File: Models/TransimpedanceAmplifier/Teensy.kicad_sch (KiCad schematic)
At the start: 5 parts, among them J11 Conn_01x24_Pin, J13 Conn_01x24_Pin, U13 Teensy4.1

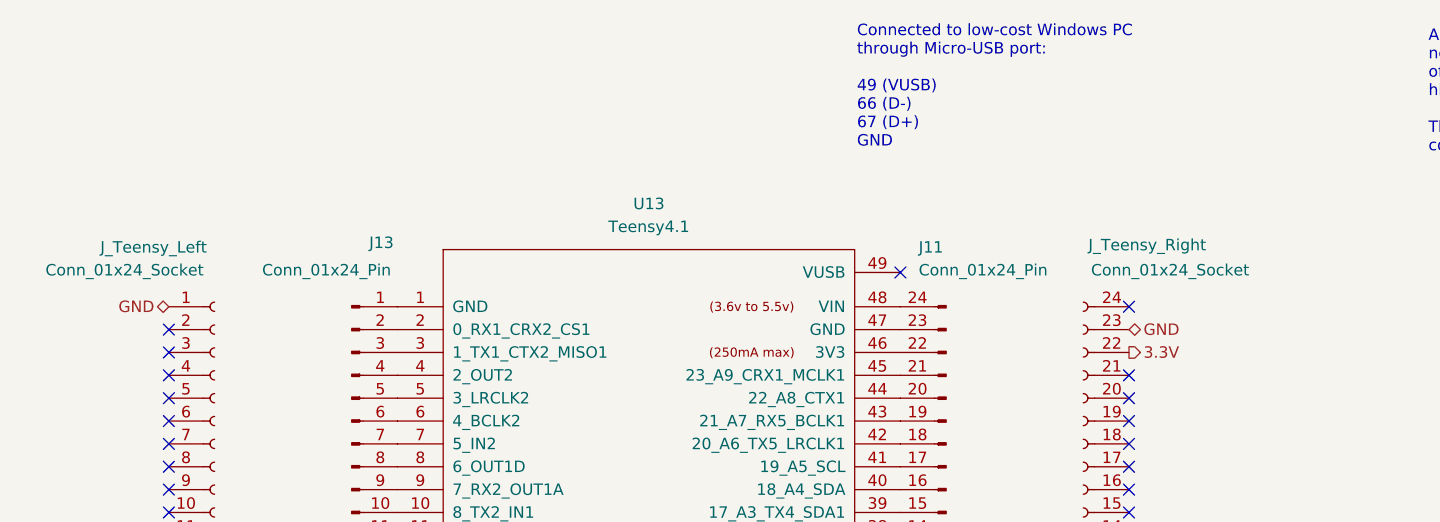
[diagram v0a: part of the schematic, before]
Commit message: Overhauled all of the annotations
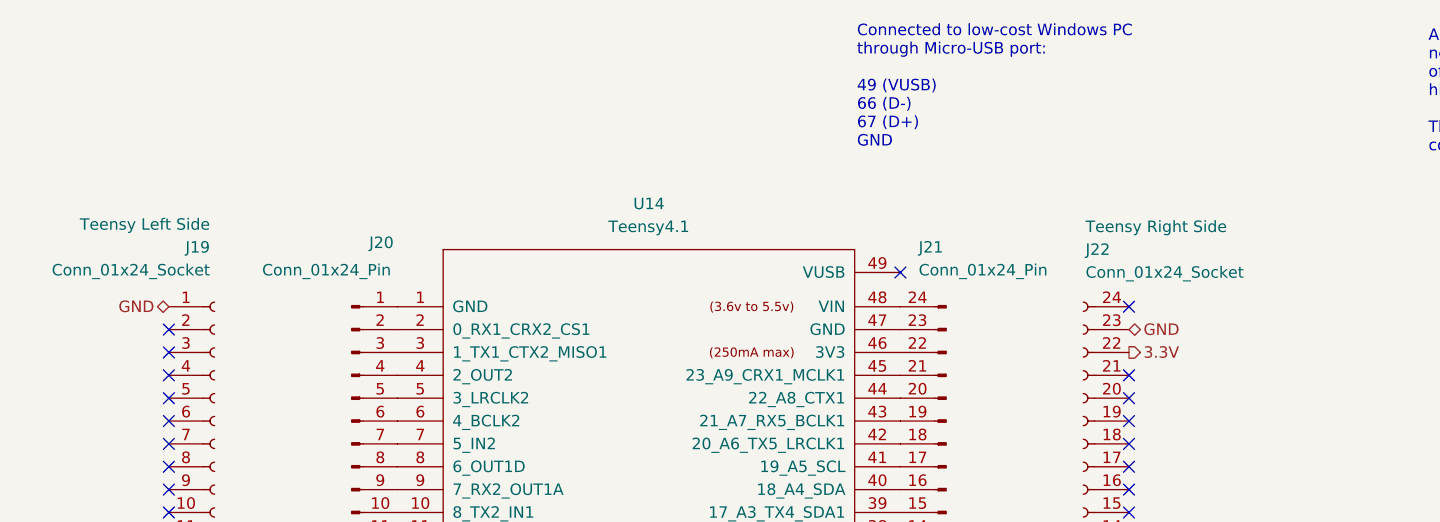
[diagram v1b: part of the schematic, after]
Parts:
- renumbered J_Teensy_Left to J19, J13 to J20, J11 to J21, J_Teensy_Right to J22, U13 to U14
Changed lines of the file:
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@@
 		(on_board yes)
 		(dnp no)
-		(property "Reference" "J_Teensy_Right"
-			(at 159.512 62.992 0)
-			(effects
-				(font
-					(size 1.27 1.27)
-				)
+		(property "Reference" "J22"
+			(at 152.654 63.5 0)
+			(effects
+				(font
+					(size 1.27 1.27)
+				)
+				(justify right)
 			)
 		)
 		(property "Value" "Conn_01x24_Socket"
-			(at 162.052 65.786 0)
-			(effects
-				(font
-					(size 1.27 1.27)
-				)
+			(at 152.654 66.04 0)
+			(effects
+				(font
+					(size 1.27 1.27)
+				)
+				(justify right)
 			)
 		)
@@
 			)
 		)
-		(property "Description" "Generic connector, single row, 01x24, script generated"
-			(at 152.4 100.33 0)
-			(effects
-				(font
-					(size 1.27 1.27)
-				)
-				(hide yes)
+		(property "Description" "Teensy Right Side"
+			(at 152.654 60.96 0)
+			(effects
+				(font
+					(size 1.27 1.27)
+				)
+				(justify right)
 			)
 		)
@@
 			(project ""
 				(path "/ec9f2ae3-e40d-40eb-9760-2b611ee8efd1/7e303428-a18c-4ad4-b002-5ab9c6631588/801eb825-6f09-44eb-9a12-14faa51f83f1"
-					(reference "J_Teensy_Right")
+					(reference "J22")
 					(unit 1)
 				)
@@
 		(on_board yes)
 		(dnp no)
-		(property "Reference" "J_Teensy_Left"
-			(at 43.18 63.246 0)
-			(effects
-				(font
-					(size 1.27 1.27)
-				)
-				(justify left)
+		(property "Reference" "J19"
+			(at 55.372 63.246 0)
+			(effects
+				(font
+					(size 1.27 1.27)
+				)
+				(justify right)
 			)
 		)
 		(property "Value" "Conn_01x24_Socket"
-			(at 37.084 65.786 0)
-			(effects
-				(font
-					(size 1.27 1.27)
-				)
-				(justify left)
+			(at 55.372 65.786 0)
+			(effects
+				(font
+					(size 1.27 1.27)
+				)
+				(justify right)
 			)
 		)
@@
 			)
 		)
-		(property "Description" "Generic connector, single row, 01x24, script generated"
-			(at 55.88 97.79 0)
-			(effects
-				(font
-					(size 1.27 1.27)
-				)
-				(hide yes)
+		(property "Description" "Teensy Left Side"
+			(at 55.372 60.706 0)
+			(effects
+				(font
+					(size 1.27 1.27)
+				)
+				(justify right)
 			)
 		)
@@
 			(project ""
 				(path "/ec9f2ae3-e40d-40eb-9760-2b611ee8efd1/7e303428-a18c-4ad4-b002-5ab9c6631588/801eb825-6f09-44eb-9a12-14faa51f83f1"
-					(reference "J_Teensy_Left")
+					(reference "J19")
 					(unit 1)
 				)
@@
 		(on_board no)
 		(dnp no)
-		(property "Reference" "J13"
+		(property "Reference" "J20"
 			(at 74.422 62.738 0)
 			(effects
@@
 			(project ""
 				(path "/ec9f2ae3-e40d-40eb-9760-2b611ee8efd1/7e303428-a18c-4ad4-b002-5ab9c6631588/801eb825-6f09-44eb-9a12-14faa51f83f1"
-					(reference "J13")
+					(reference "J20")
 					(unit 1)
 				)
@@
 		(on_board no)
 		(dnp no)
-		(property "Reference" "J11"
+		(property "Reference" "J21"
 			(at 134.112 63.246 0)
 			(effects
@@
 			(project ""
 				(path "/ec9f2ae3-e40d-40eb-9760-2b611ee8efd1/7e303428-a18c-4ad4-b002-5ab9c6631588/801eb825-6f09-44eb-9a12-14faa51f83f1"
-					(reference "J11")
+					(reference "J21")
 					(unit 1)
 				)
@@
 		(dnp no)
 		(fields_autoplaced yes)
-		(property "Reference" "U13"
+		(property "Reference" "U14"
 			(at 104.14 58.42 0)
 			(effects
@@
 			(project "TransimpedanceAmplifier"
 				(path "/ec9f2ae3-e40d-40eb-9760-2b611ee8efd1/7e303428-a18c-4ad4-b002-5ab9c6631588/801eb825-6f09-44eb-9a12-14faa51f83f1"
-					(reference "U13")
+					(reference "U14")
 					(unit 1)
 				)

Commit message: Completely fixed the batteries
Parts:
- renumbered J19 to J11, J20 to J12, J21 to J13, J22 to J14
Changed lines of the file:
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@@
 		(on_board yes)
 		(dnp no)
-		(property "Reference" "J22"
+		(property "Reference" "J14"
 			(at 152.654 63.5 0)
 			(effects
@@
 			(project ""
 				(path "/ec9f2ae3-e40d-40eb-9760-2b611ee8efd1/7e303428-a18c-4ad4-b002-5ab9c6631588/801eb825-6f09-44eb-9a12-14faa51f83f1"
-					(reference "J22")
+					(reference "J14")
 					(unit 1)
 				)
@@
 		(on_board yes)
 		(dnp no)
-		(property "Reference" "J19"
+		(property "Reference" "J11"
 			(at 55.372 63.246 0)
 			(effects
@@
 			(project ""
 				(path "/ec9f2ae3-e40d-40eb-9760-2b611ee8efd1/7e303428-a18c-4ad4-b002-5ab9c6631588/801eb825-6f09-44eb-9a12-14faa51f83f1"
-					(reference "J19")
+					(reference "J11")
 					(unit 1)
 				)
@@
 		(on_board no)
 		(dnp no)
-		(property "Reference" "J20"
+		(property "Reference" "J12"
 			(at 74.422 62.738 0)
 			(effects
@@
 			(project ""
 				(path "/ec9f2ae3-e40d-40eb-9760-2b611ee8efd1/7e303428-a18c-4ad4-b002-5ab9c6631588/801eb825-6f09-44eb-9a12-14faa51f83f1"
-					(reference "J20")
+					(reference "J12")
 					(unit 1)
 				)
@@
 		(on_board no)
 		(dnp no)
-		(property "Reference" "J21"
+		(property "Reference" "J13"
 			(at 134.112 63.246 0)
 			(effects
@@
 			(project ""
 				(path "/ec9f2ae3-e40d-40eb-9760-2b611ee8efd1/7e303428-a18c-4ad4-b002-5ab9c6631588/801eb825-6f09-44eb-9a12-14faa51f83f1"
-					(reference "J21")
+					(reference "J13")
 					(unit 1)
 				)

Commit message: Working on filling in the last details of the schematics
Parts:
- J11, J12, J13, J14, U14: Cost (none) -> $0.00; RoHS Compliant (none) -> NO
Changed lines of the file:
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@@
+			)
+		)
+		(property "Cost" "$0.00"
+			(at 152.4 100.33 0)
+			(effects
+				(font
+					(size 1.27 1.27)
+				)
+				(hide yes)
+			)
+		)
+		(property "RoHS Compliant" "NO"
+			(at 152.4 100.33 0)
+			(effects
+				(font
+					(size 1.27 1.27)
+				)
+				(hide yes)
 			)
 		)
@@
 			)
 		)
+		(property "Cost" "$0.00"
+			(at 55.88 97.79 0)
+			(effects
+				(font
+					(size 1.27 1.27)
+				)
+				(hide yes)
+			)
+		)
+		(property "RoHS Compliant" "NO"
+			(at 55.88 97.79 0)
+			(effects
+				(font
+					(size 1.27 1.27)
+				)
+				(hide yes)
+			)
+		)
 		(pin "2"
 		)
@@
 			)
 		)
+		(property "Cost" "$0.00"
+			(at 71.12 97.79 0)
+			(effects
+				(font
+					(size 1.27 1.27)
+				)
+				(hide yes)
+			)
+		)
+		(property "RoHS Compliant" "NO"
+			(at 71.12 97.79 0)
+			(effects
+				(font
+					(size 1.27 1.27)
+				)
+				(hide yes)
+			)
+		)
 		(pin "2"
 		)
@@
 		)
 		(property "Purchase Link" "https://www.digikey.com/en/products/detail/sullins-connector-solutions/PRPC024SAAN-RC/2775230"
+			(at 137.16 100.33 0)
+			(effects
+				(font
+					(size 1.27 1.27)
+				)
+				(hide yes)
+			)
+		)
+		(property "Cost" "$0.00"
+			(at 137.16 100.33 0)
+			(effects
+				(font
+					(size 1.27 1.27)
+				)
+				(hide yes)
+			)
+		)
+		(property "RoHS Compliant" "NO"
 			(at 137.16 100.33 0)
 			(effects
@@
 			(at 104.14 124.46 0)
 			(effects
+				(font
+					(size 1.27 1.27)
+				)
+				(hide yes)
+			)
+		)
+		(property "Cost" "$0.00"
+			(at 104.14 124.46 0)
+			(effects
+				(font
+					(size 1.27 1.27)
+				)
+				(hide yes)
+			)
+		)
+		(property "RoHS Compliant" "NO"
+			(at 104.14 124.46 0)
+			(effects

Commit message: Fixed a bug in footprint assignment
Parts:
- J11, J14: footprint (none) -> Connector_Custom:PinSocket_1x24
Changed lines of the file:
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@@
 			)
 		)
-		(property "Footprint" ""
+		(property "Footprint" "Connector_Custom:PinSocket_1x24"
 			(at 152.4 100.33 0)
 			(effects
@@
 			)
 		)
-		(property "Footprint" ""
+		(property "Footprint" "Connector_Custom:PinSocket_1x24"
 			(at 55.88 97.79 0)
 			(effects

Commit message: Save progress
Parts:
- J11, J14: Cost $0.00 -> $1.35; Cost (qty10) (none) -> $1.144; RoHS Compliant NO -> YES
- J12, J13: Cost $0.00 -> $0.66; Cost (qty10) (none) -> $0.563; RoHS Compliant NO -> YES
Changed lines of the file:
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@@
 			)
 		)
-		(property "Cost" "$0.00"
+		(property "Cost" "$1.35"
 			(at 152.4 100.33 0)
 			(effects
@@
 			)
 		)
-		(property "RoHS Compliant" "NO"
+		(property "RoHS Compliant" "YES"
+			(at 152.4 100.33 0)
+			(effects
+				(font
+					(size 1.27 1.27)
+				)
+				(hide yes)
+			)
+		)
+		(property "Cost (qty10)" "$1.144"
 			(at 152.4 100.33 0)
 			(effects
@@
 			)
 		)
-		(property "Cost" "$0.00"
-			(at 55.88 97.79 0)
-			(effects
-				(font
-					(size 1.27 1.27)
-				)
-				(hide yes)
-			)
-		)
-		(property "RoHS Compliant" "NO"
+		(property "Cost" "$1.35"
+			(at 55.88 97.79 0)
+			(effects
+				(font
+					(size 1.27 1.27)
+				)
+				(hide yes)
+			)
+		)
+		(property "RoHS Compliant" "YES"
+			(at 55.88 97.79 0)
+			(effects
+				(font
+					(size 1.27 1.27)
+				)
+				(hide yes)
+			)
+		)
+		(property "Cost (qty10)" "$1.144"
 			(at 55.88 97.79 0)
 			(effects
@@
 			)
 		)
-		(property "Cost" "$0.00"
-			(at 71.12 97.79 0)
-			(effects
-				(font
-					(size 1.27 1.27)
-				)
-				(hide yes)
-			)
-		)
-		(property "RoHS Compliant" "NO"
+		(property "Cost" "$0.66"
+			(at 71.12 97.79 0)
+			(effects
+				(font
+					(size 1.27 1.27)
+				)
+				(hide yes)
+			)
+		)
+		(property "RoHS Compliant" "YES"
+			(at 71.12 97.79 0)
+			(effects
+				(font
+					(size 1.27 1.27)
+				)
+				(hide yes)
+			)
+		)
+		(property "Cost (qty10)" "$0.563"
 			(at 71.12 97.79 0)
 			(effects
@@
 			)
 		)
-		(property "Cost" "$0.00"
-			(at 137.16 100.33 0)
-			(effects
-				(font
-					(size 1.27 1.27)
-				)
-				(hide yes)
-			)
-		)
-		(property "RoHS Compliant" "NO"
-			(at 137.16 100.33 0)
-			(effects
+		(property "Cost" "$0.66"
+			(at 137.16 100.33 0)
+			(effects
+				(font
+					(size 1.27 1.27)
+				)
+				(hide yes)
+			)
+		)
+		(property "RoHS Compliant" "YES"
+			(at 137.16 100.33 0)
+			(effects
+				(font
+					(size 1.27 1.27)
+				)
+				(hide yes)
+			)
+		)
+		(property "Cost (qty10)" "$0.563"
+			(at 137.16 100.33 0)
+			(effects

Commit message: Added important links regarding high-voltage electronics
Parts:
- U14: Cost $0.00 -> $29.60; Purchase Link (none) -> https://www.sparkfun.com/teensy-4-1-without-ethernet.html; RoHS Compliant NO -> YES
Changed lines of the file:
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@@
 			)
 		)
-		(property "Purchase Link" ""
+		(property "Purchase Link" "https://www.sparkfun.com/teensy-4-1-without-ethernet.html"
 			(at 104.14 124.46 0)
 			(effects
@@
 			)
 		)
-		(property "Cost" "$0.00"
+		(property "Cost" "$29.60"
 			(at 104.14 124.46 0)
 			(effects
@@
 			)
 		)
-		(property "RoHS Compliant" "NO"
+		(property "RoHS Compliant" "YES"
 			(at 104.14 124.46 0)
 			(effects

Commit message: Starting major changes in response to the SOIC-8 version of OP37 being out of stock
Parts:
- U14: Cost (qty10) (none) -> $29.60
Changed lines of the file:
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@@
+			)
+		)
+		(property "Cost (qty10)" "$29.60"
+			(at 104.14 124.46 0)
+			(effects
+				(font
+					(size 1.27 1.27)
+				)
+				(hide yes)
 			)
 		)

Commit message: Commit project
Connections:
- net 3.3V: no longer J11.15 (Pin_15)
- no-connect marks 57 -> 58
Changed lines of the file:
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@@
+	)
+	(no_connect
+		(at 50.8 105.41)
 	)
 	(no_connect
@@
 		(effects
 			(font
-				(size 1.27 1.27)
-			)
-			(justify right)
-		)
-	)
-	(hierarchical_label "3.3V"
-		(shape output)
-		(at 50.8 105.41 180)
-		(effects
-			(font
